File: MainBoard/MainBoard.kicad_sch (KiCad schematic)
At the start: 13 parts, among them J1 Conn_01x20, J10 Conn_01x04, J2 Conn_01x12, J3 Conn_01x10, J4 Conn_01x07, J5 Conn_01x06, J6 Conn_01x06, J7 Conn_01x06, J8 Conn_01x06, J9 Conn_01x04

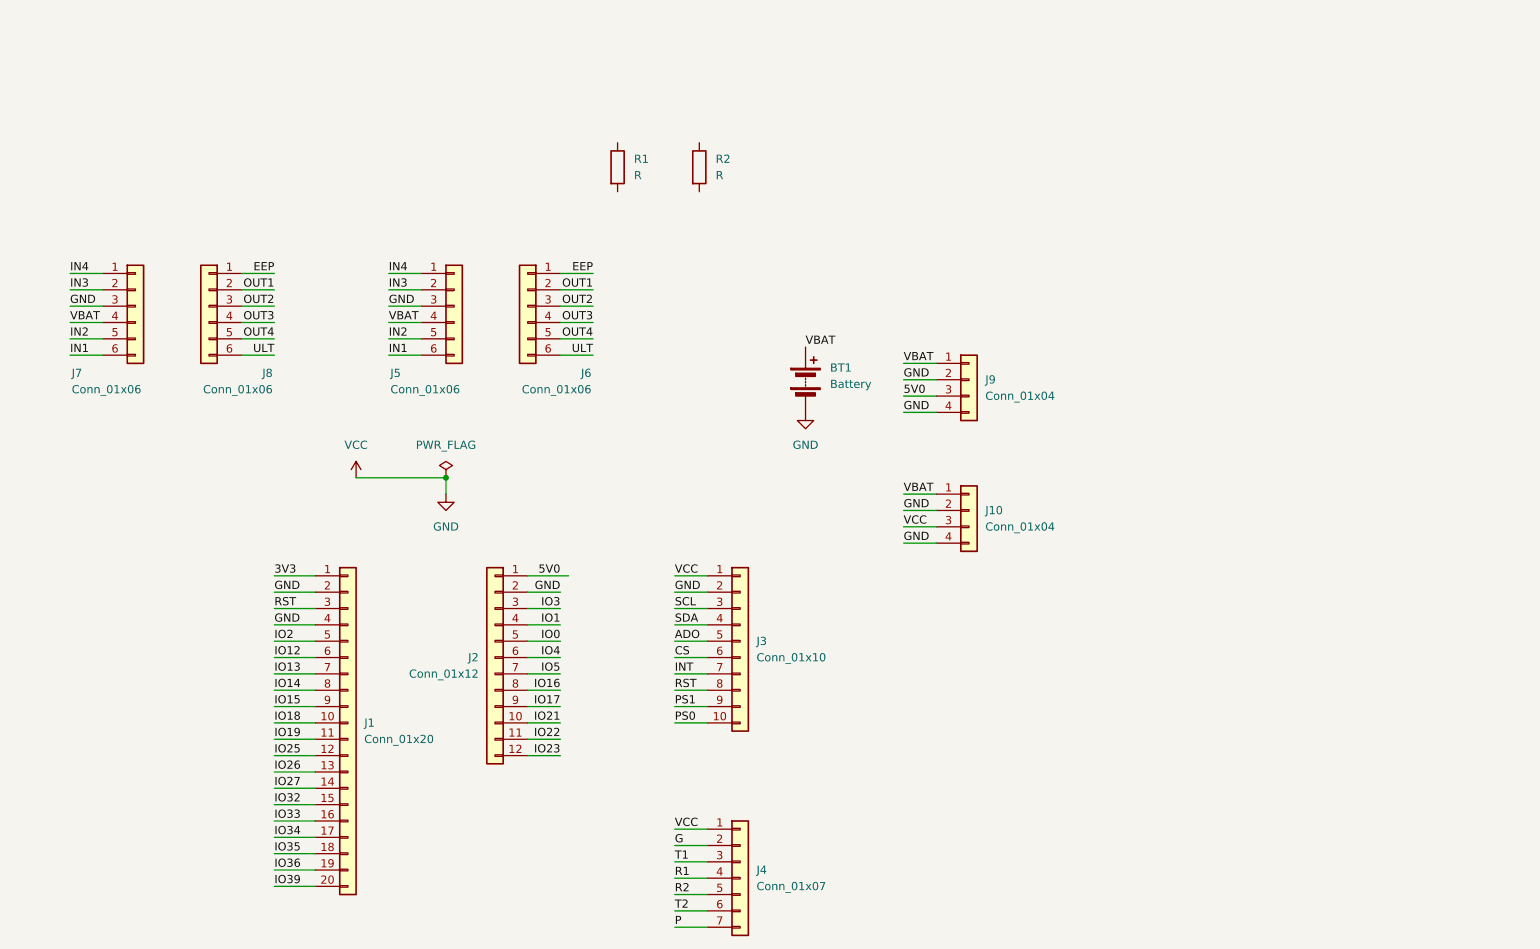
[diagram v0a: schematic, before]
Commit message: 회로도 -> 풋프린트 완료 PCB편집기 제작 시작
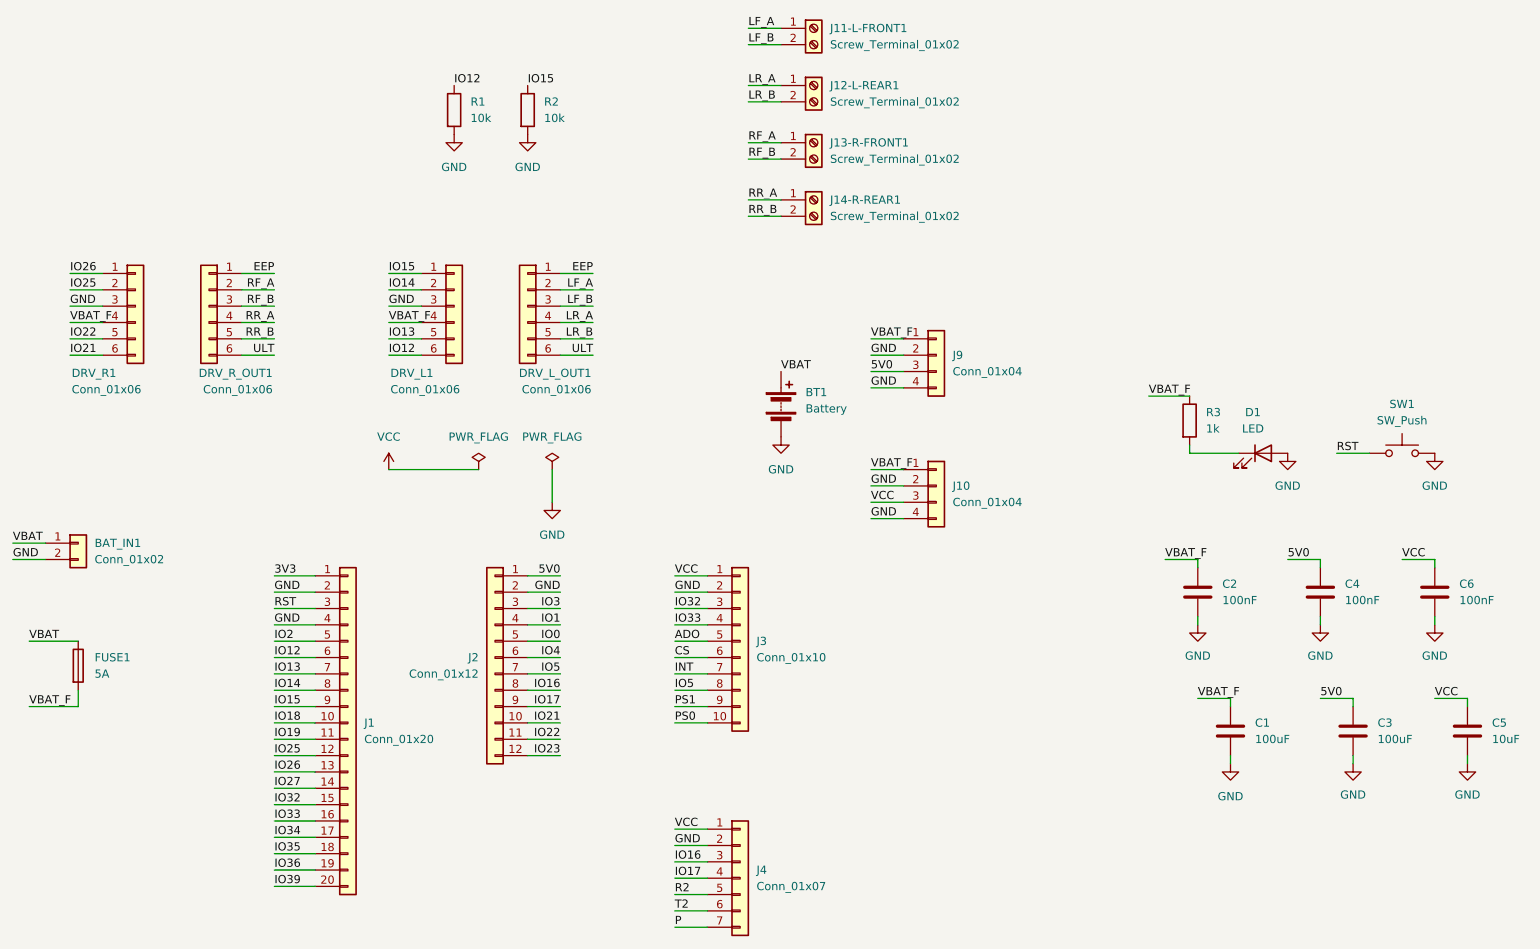
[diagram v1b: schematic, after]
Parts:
- added BAT_IN1: Conn_01x02, Connector_AMASS:AMASS_XT30UPB-F_1x02_P5.0mm_Vertical, symbol Connector_Generic:Conn_01x02
- added C1, C3: 100uF, Capacitor_THT:CP_Radial_D6.3mm_P2.50mm, symbol Device:C
- added C2, C4, C6: 100nF, Capacitor_THT:C_Disc_D5.0mm_W2.5mm_P5.00mm, symbol Device:C
- added C5: 10uF, Capacitor_THT:CP_Radial_D5.0mm_P2.50mm, symbol Device:C
- added D1: LED, LED_THT:LED_D5.0mm, symbol Device:LED
- added FUSE1: 5A, Fuse:Fuseholder_Cylinder-5x20mm_Schurter_0031_8201_Horizontal_Open, symbol Device:Fuse
- added J11-L-FRONT1, J12-L-REAR1, J13-R-FRONT1, J14-R-REAR1: Screw_Terminal_01x02, Connector_Phoenix_MSTB:PhoenixContact_MSTBA_2,5_2-G-5,08_1x02_P5.08mm_Horizontal, symbol Connector:Screw_Terminal_01x02
- added R3: 1k, Resistor_THT:R_Axial_DIN0204_L3.6mm_D1.6mm_P7.62mm_Horizontal, symbol Device:R
- added SW1: SW_Push, Button_Switch_THT:SW_PUSH_6mm, symbol Switch:SW_Push
- DRV_L1: renamed from J5; footprint (none) -> Connector_PinSocket_2.54mm:PinSocket_1x06_P2.54mm_Vertical
- DRV_L_OUT1: renamed from J6; footprint (none) -> Connector_PinSocket_2.54mm:PinSocket_1x06_P2.54mm_Vertical
- DRV_R1: renamed from J7; footprint (none) -> Connector_PinSocket_2.54mm:PinSocket_1x06_P2.54mm_Vertical
- DRV_R_OUT1: renamed from J8; footprint (none) -> Connector_PinSocket_2.54mm:PinSocket_1x06_P2.54mm_Vertical
- J1: footprint (none) -> Connector_PinSocket_2.54mm:PinSocket_1x20_P2.54mm_Vertical
- J10, J9: footprint (none) -> Connector_PinSocket_2.54mm:PinSocket_1x04_P2.54mm_Vertical
- J2: footprint (none) -> Connector_PinSocket_2.54mm:PinSocket_1x12_P2.54mm_Vertical
- J3: footprint (none) -> Connector_PinSocket_2.54mm:PinSocket_1x10_P2.54mm_Vertical
- J4: footprint (none) -> Connector_PinSocket_2.54mm:PinSocket_1x07_P2.54mm_Vertical
- R1, R2: value R -> 10k; footprint (none) -> Resistor_THT:R_Axial_DIN0204_L3.6mm_D1.6mm_P7.62mm_Horizontal
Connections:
- net G is gone; now on net GND: J4.2 (Pin_2)
- net R1 is gone; now on net IO17: J4.4 (Pin_4)
- net SCL is gone; now on net IO32: J3.3 (Pin_3)
- net SDA is gone; now on net IO33: J3.4 (Pin_4)
- net T1 is gone; now on net IO16: J4.3 (Pin_3)
- net 5V0: now also C3.1, C4.1
- net GND: now also R1.2, R2.2, BAT_IN1.2 (Pin_2), C1.2, C2.2, C3.2, C4.2, C5.2, C6.2, D1.2 (A), SW1.2; no longer J10.3 (Pin_3), J3.1 (Pin_1), J4.1 (Pin_1)
- net IO12: now also DRV_L1.6 (Pin_6), R1.1
- net IO13: now also DRV_L1.5 (Pin_5)
- net IO14: now also DRV_L1.2 (Pin_2)
- net IO15: now also DRV_L1.1 (Pin_1), R2.1
- net IO21: now also DRV_R1.6 (Pin_6)
- net IO22: now also DRV_R1.5 (Pin_5)
- net IO25: now also DRV_R1.2 (Pin_2)
- net IO26: now also DRV_R1.1 (Pin_1)
- net IO5: now also J3.8 (Pin_8)
- net RST: now also SW1.1; no longer J3.8 (Pin_8)
- net VBAT: now also BAT_IN1.1 (Pin_1), FUSE1.1; no longer DRV_L1.4 (Pin_4), DRV_R1.4 (Pin_4), J10.1 (Pin_1), J9.1 (Pin_1)
- removed net IN1: DRV_L1.6 (Pin_6), DRV_R1.6 (Pin_6)
- removed net IN2: DRV_L1.5 (Pin_5), DRV_R1.5 (Pin_5)
- removed net IN3: DRV_L1.2 (Pin_2), DRV_R1.2 (Pin_2)
- removed net IN4: DRV_L1.1 (Pin_1), DRV_R1.1 (Pin_1)
- net OUT1 renamed LF_A
- net LF_A: now also J11-L-FRONT1.1 (Pin_1); no longer DRV_R_OUT1.2 (Pin_2)
- net OUT2 renamed LF_B
- net LF_B: now also J11-L-FRONT1.2 (Pin_2); no longer DRV_R_OUT1.3 (Pin_3)
- net OUT3 renamed LR_A
- net LR_A: now also J12-L-REAR1.1 (Pin_1); no longer DRV_R_OUT1.4 (Pin_4)
- net OUT4 renamed LR_B
- net LR_B: now also J12-L-REAR1.2 (Pin_2); no longer DRV_R_OUT1.5 (Pin_5)
- new net: D1.1 (K), R3.2
- new net RF_A: DRV_R_OUT1.2 (Pin_2), J13-R-FRONT1.1 (Pin_1)
- new net RF_B: DRV_R_OUT1.3 (Pin_3), J13-R-FRONT1.2 (Pin_2)
- new net RR_A: DRV_R_OUT1.4 (Pin_4), J14-R-REAR1.1 (Pin_1)
- new net RR_B: DRV_R_OUT1.5 (Pin_5), J14-R-REAR1.2 (Pin_2)
- new net VBAT_F: C1.1, C2.1, DRV_L1.4 (Pin_4), DRV_R1.4 (Pin_4), FUSE1.2, J10.1 (Pin_1), J9.1 (Pin_1), R3.1
- new net VCC: C5.1, C6.1, J10.3 (Pin_3), J3.1 (Pin_1), J4.1 (Pin_1)
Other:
- moved on the sheet: BT1, J10, J9, R1, R2

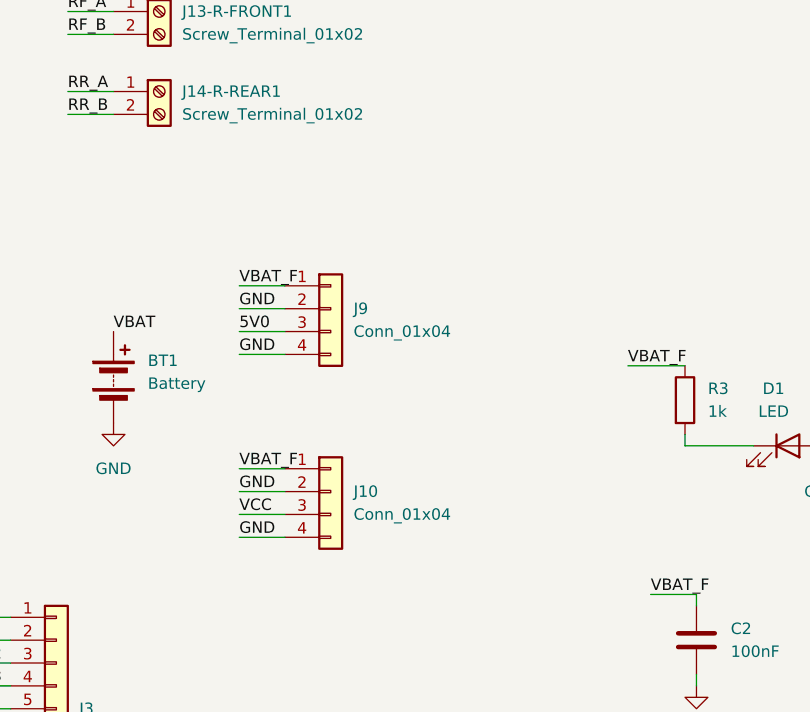
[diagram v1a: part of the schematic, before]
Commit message: mini360_mp1584en회로수정
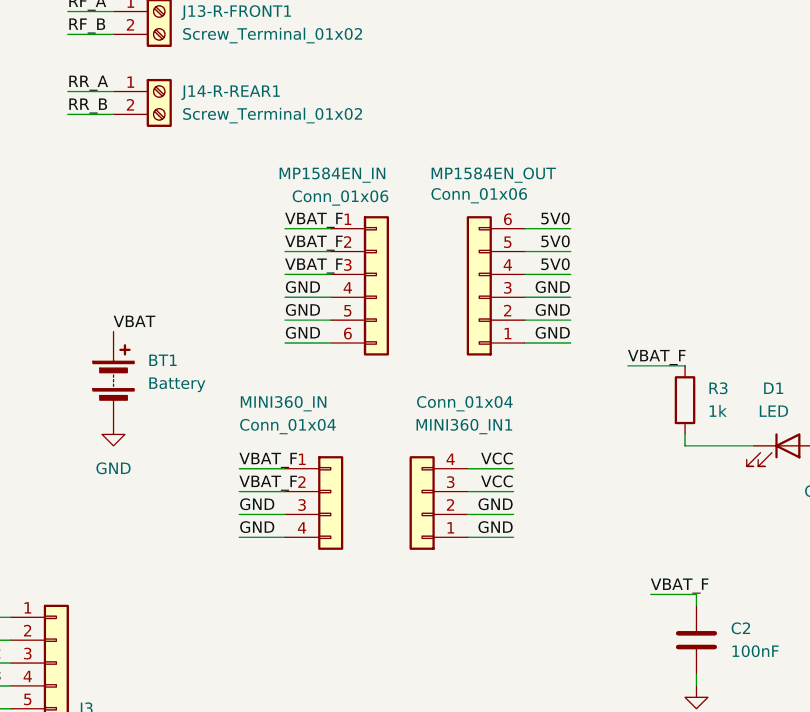
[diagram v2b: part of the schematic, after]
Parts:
- removed J9: Conn_01x04, Connector_PinSocket_2.54mm:PinSocket_1x04_P2.54mm_Vertical, symbol Connector_Generic:Conn_01x04
- added MINI360_IN1: Conn_01x04, Connector_PinSocket_2.54mm:PinSocket_1x04_P2.54mm_Vertical, symbol Connector_Generic:Conn_01x04
- added MP1584EN_IN, MP1584EN_OUT: Conn_01x06, symbol Connector_Generic:Conn_01x06
- renumbered J10 to MINI360_IN
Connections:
- net 5V0: now also MP1584EN_OUT.4 (Pin_4), MP1584EN_OUT.5 (Pin_5), MP1584EN_OUT.6 (Pin_6)
- net GND: now also MINI360_IN.3 (Pin_3), MINI360_IN1.1 (Pin_1), MINI360_IN1.2 (Pin_2), MP1584EN_IN.4 (Pin_4), MP1584EN_IN.5 (Pin_5), MP1584EN_IN.6 (Pin_6), MP1584EN_OUT.1 (Pin_1), MP1584EN_OUT.2 (Pin_2), MP1584EN_OUT.3 (Pin_3); no longer MINI360_IN.2 (Pin_2)
- net VBAT_F: now also MINI360_IN.2 (Pin_2), MP1584EN_IN.1 (Pin_1), MP1584EN_IN.2 (Pin_2), MP1584EN_IN.3 (Pin_3)
- net VCC: now also MINI360_IN1.3 (Pin_3), MINI360_IN1.4 (Pin_4); no longer MINI360_IN.3 (Pin_3)
